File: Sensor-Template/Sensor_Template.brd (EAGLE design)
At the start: 20 x 24.1 mm, 2 parts, among them J1 TWIG-2.0-DIP

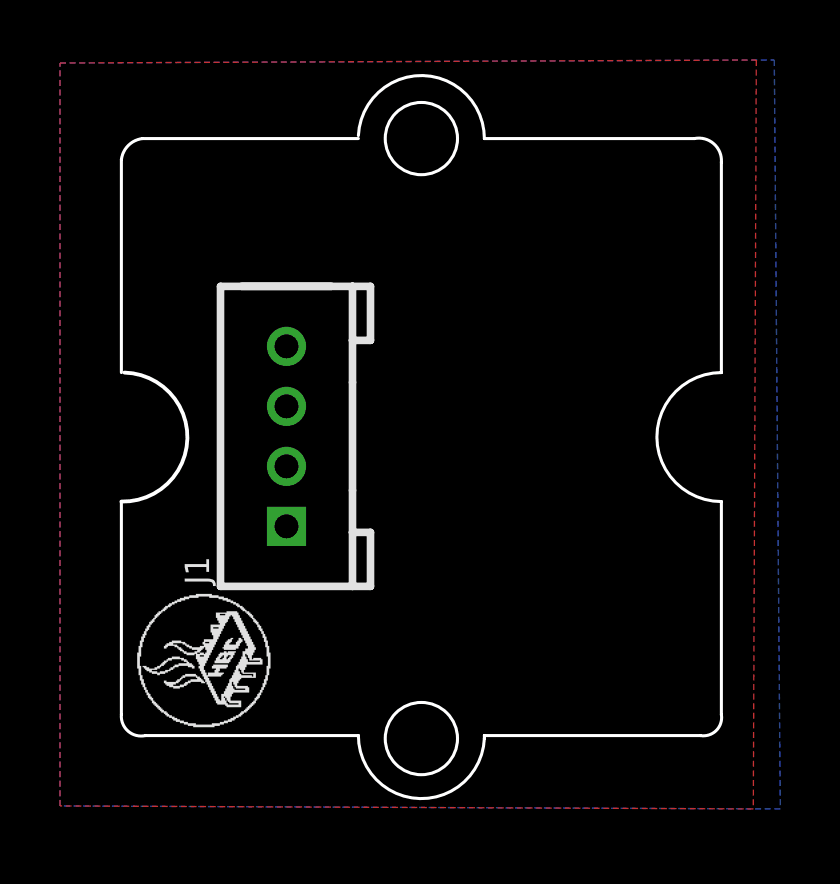
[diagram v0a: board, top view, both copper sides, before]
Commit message: Revised Sensor Template
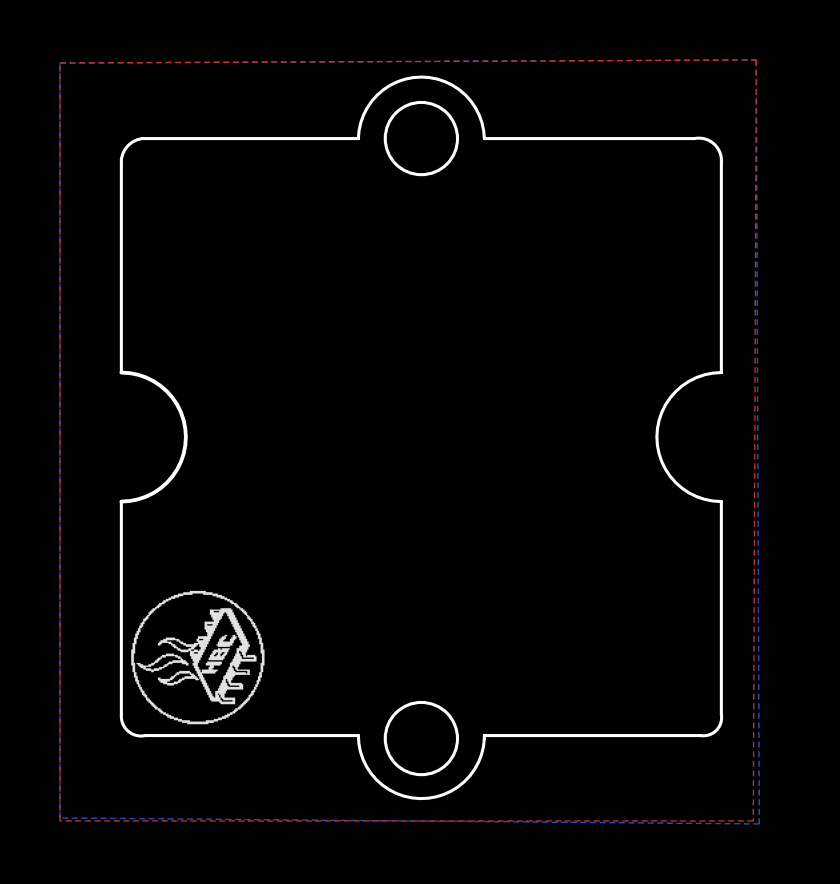
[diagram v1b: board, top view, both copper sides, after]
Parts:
- removed J1: TWIG-2.0-DIP, Connector:2.0_1X4
- moved U$1 0.22 mm to (7.05, 3.00)
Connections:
- removed net DATA: J1.1
- removed net GND: J1.4
- removed net VCC: J1.3
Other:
- outline, holes or cut-outs redrawn
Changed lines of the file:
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@@
 <layer number="43" name="vRestrict" color="2" fill="10" visible="yes" active="yes"/>
 <layer number="44" name="Drills" color="7" fill="1" visible="no" active="yes"/>
-<layer number="45" name="Holes" color="7" fill="1" visible="no" active="yes"/>
+<layer number="45" name="Holes" color="7" fill="1" visible="yes" active="yes"/>
 <layer number="46" name="Milling" color="3" fill="1" visible="no" active="yes"/>
 <layer number="47" name="Measures" color="7" fill="1" visible="no" active="yes"/>
@@
 <layer number="54" name="bGND_GNDA" color="1" fill="9" visible="no" active="no"/>
 <layer number="56" name="wert" color="7" fill="1" visible="no" active="yes"/>
+<layer number="57" name="tCAD" color="7" fill="1" visible="yes" active="yes"/>
+<layer number="59" name="tCarbon" color="7" fill="1" visible="yes" active="yes"/>
+<layer number="60" name="bCarbon" color="7" fill="1" visible="yes" active="yes"/>
 <layer number="90" name="Modules" color="5" fill="1" visible="no" active="no"/>
 <layer number="91" name="Nets" color="2" fill="1" visible="no" active="no"/>
@@
 <layer number="97" name="Info" color="7" fill="1" visible="no" active="no"/>
 <layer number="98" name="Guide" color="6" fill="1" visible="no" active="no"/>
+<layer number="99" name="SpiceOrder" color="7" fill="1" visible="no" active="no"/>
 <layer number="100" name="Muster" color="7" fill="1" visible="no" active="no"/>
 <layer number="101" name="DISIGN_HISTORY" color="3" fill="1" visible="no" active="yes"/>
@@
 <layer number="106" name="bPlate" color="7" fill="1" visible="yes" active="yes"/>
 <layer number="107" name="Crop" color="7" fill="1" visible="yes" active="yes"/>
+<layer number="108" name="centerline" color="7" fill="1" visible="yes" active="yes"/>
+<layer number="109" name="ref-old" color="7" fill="1" visible="yes" active="yes"/>
+<layer number="110" name="fp0" color="7" fill="1" visible="yes" active="yes"/>
+<layer number="111" name="LPC17xx" color="7" fill="1" visible="yes" active="yes"/>
+<layer number="112" name="tSilk" color="7" fill="1" visible="yes" active="yes"/>
+<layer number="113" name="IDFDebug" color="7" fill="1" visible="yes" active="yes"/>
+<layer number="114" name="Badge_Outline" color="7" fill="1" visible="yes" active="yes"/>
+<layer number="115" name="ReferenceISLANDS" color="7" fill="1" visible="yes" active="yes"/>
 <layer number="116" name="Patch_BOT" color="9" fill="4" visible="no" active="yes"/>
+<layer number="118" name="Rect_Pads" color="7" fill="1" visible="yes" active="yes"/>
 <layer number="121" name="_tsilk" color="7" fill="1" visible="no" active="yes"/>
 <layer number="122" name="_bsilk" color="7" fill="1" visible="no" active="yes"/>
+<layer number="123" name="tTestmark" color="7" fill="1" visible="yes" active="yes"/>
+<layer number="124" name="bTestmark" color="7" fill="1" visible="yes" active="yes"/>
+<layer number="125" name="_tNames" color="7" fill="1" visible="yes" active="yes"/>
+<layer number="126" name="_bNames" color="7" fill="1" visible="yes" active="yes"/>
+<layer number="127" name="_tValues" color="7" fill="1" visible="yes" active="yes"/>
+<layer number="128" name="_bValues" color="7" fill="1" visible="yes" active="yes"/>
+<layer number="129" name="Mask" color="7" fill="1" visible="yes" active="yes"/>
+<layer number="131" name="prix" color="7" fill="1" visible="yes" active="yes"/>
+<layer number="132" name="test" color="7" fill="1" visible="yes" active="yes"/>
 <layer number="144" name="DrillLegend" color="7" fill="1" visible="no" active="yes"/>
+<layer number="150" name="Notes" color="7" fill="1" visible="yes" active="yes"/>
 <layer number="151" name="HeatSink" color="14" fill="1" visible="no" active="no"/>
+<layer number="152" name="_bDocu" color="7" fill="1" visible="yes" active="yes"/>
+<layer number="153" name="FabDoc1" color="7" fill="1" visible="yes" active="yes"/>
+<layer number="154" name="FabDoc2" color="7" fill="1" visible="yes" active="yes"/>
+<layer number="155" name="FabDoc3" color="7" fill="1" visible="yes" active="yes"/>
+<layer number="156" name="tAssmbl" color="7" fill="1" visible="yes" active="yes"/>
+<layer number="157" name="bAssmbl" color="7" fill="1" visible="yes" active="yes"/>
+<layer number="199" name="Contour" color="7" fill="1" visible="yes" active="yes"/>
 <layer number="200" name="200bmp" color="1" fill="10" visible="no" active="no"/>
 <layer number="201" name="201bmp" color="2" fill="1" visible="no" active="no"/>
@@
 <layer number="215" name="215bmp" color="7" fill="1" visible="yes" active="yes"/>
 <layer number="216" name="216bmp" color="7" fill="1" visible="yes" active="yes"/>
+<layer number="217" name="217bmp" color="7" fill="1" visible="yes" active="yes"/>
+<layer number="218" name="218bmp" color="7" fill="1" visible="yes" active="yes"/>
+<layer number="219" name="219bmp" color="7" fill="1" visible="yes" active="yes"/>
+<layer number="220" name="220bmp" color="11" fill="1" visible="yes" active="yes"/>
+<layer number="221" name="221bmp" color="7" fill="1" visible="yes" active="yes"/>
+<layer number="223" name="223bmp" color="7" fill="1" visible="yes" active="yes"/>
+<layer number="224" name="224bmp" color="7" fill="1" visible="yes" active="yes"/>
+<layer number="225" name="225bmp" color="7" fill="1" visible="yes" active="yes"/>
+<layer number="226" name="226bmp" color="7" fill="1" visible="yes" active="yes"/>
+<layer number="227" name="227bmp" color="7" fill="1" visible="yes" active="yes"/>
+<layer number="228" name="228bmp" color="7" fill="1" visible="yes" active="yes"/>
+<layer number="229" name="229bmp" color="7" fill="1" visible="yes" active="yes"/>
+<layer number="230" name="230bmp" color="7" fill="1" visible="yes" active="yes"/>
+<layer number="231" name="Eagle3D_PG1" color="7" fill="1" visible="yes" active="yes"/>
+<layer number="232" name="Eagle3D_PG2" color="7" fill="1" visible="yes" active="yes"/>
+<layer number="233" name="Eagle3D_PG3" color="7" fill="1" visible="yes" active="yes"/>
+<layer number="248" name="Housing" color="7" fill="1" visible="yes" active="yes"/>
+<layer number="249" name="Edge" color="7" fill="1" visible="yes" active="yes"/>
 <layer number="250" name="Descript" color="3" fill="1" visible="no" active="no"/>
 <layer number="251" name="SMDround" color="12" fill="11" visible="no" active="no"/>
 <layer number="254" name="OrgLBR" color="13" fill="1" visible="no" active="no"/>
+<layer number="255" name="logo" color="7" fill="1" visible="yes" active="yes"/>
 </layers>
 <board>
@@
 <wire x1="14.4" y1="22.5" x2="21.4" y2="22.5" width="0.1016" layer="20"/>
 <wire x1="22.3" y1="21.7" x2="22.3" y2="14.7" width="0.1016" layer="20"/>
-<wire x1="14.4" y1="22.5" x2="10.2" y2="22.6" width="0.1016" layer="20" curve="177.278311"/>
+<wire x1="14.4" y1="22.5" x2="10.2" y2="22.5" width="0.1016" layer="20" curve="177.278311"/>
 <wire x1="22.3" y1="21.7" x2="21.4" y2="22.5" width="0.1016" layer="20" curve="106.260205"/>
 <wire x1="22.3" y1="10.4" x2="22.3" y2="3.3" width="0.1016" layer="20"/>
@@
 <circle x="12.3" y="2.5" radius="1.204159375" width="0.1016" layer="20"/>
 <circle x="12.3" y="22.5" radius="1.204159375" width="0.1016" layer="20"/>
-<wire x1="2.4" y1="14.7" x2="2.3" y2="10.4" width="0.127" layer="20" curve="-180"/>
+<wire x1="2.3" y1="14.7" x2="2.3" y2="10.4" width="0.127" layer="20" curve="-180"/>
+<hole x="12.3" y="22.5" drill="2.4"/>
+<hole x="12.3" y="2.5" drill="2.4"/>
 </plain>
 <attributes>
@@
 </autorouter>
 <elements>
-<element name="J1" library="Connector" package="2.0_1X4" value="TWIG-2.0-DIP" x="7.804" y="12.573" rot="R90"/>
-<element name="U$1" library="HalfBakedCircuits" package="HBC-LOGO-SMALL" value="HBC-LOGO-SMALL" x="7.25" y="2.9" rot="R90"/>
+<element name="U$1" library="HalfBakedCircuits" package="HBC-LOGO-SMALL" value="HBC-LOGO-SMALL" x="7.05" y="3" rot="R90"/>
 </elements>
 <signals>
-<signal name="DATA">
-<contactref element="J1" pad="1"/>
-</signal>
-<signal name="VCC">
-<contactref element="J1" pad="3"/>
-</signal>
 <signal name="GND">
-<contactref element="J1" pad="4"/>
 <polygon width="0.254" layer="16" isolate="0.3048">
-<vertex x="24.264" y="0.154"/>
-<vertex x="0.254" y="0.254"/>
+<vertex x="23.564" y="-0.346"/>
+<vertex x="0.254" y="-0.146"/>
 <vertex x="0.254" y="25.019"/>
-<vertex x="24.064" y="25.119"/>
+<vertex x="23.464" y="25.119"/>
 </polygon>
 <polygon width="0.254" layer="1" isolate="0.3048">
-<vertex x="23.364" y="0.154"/>
-<vertex x="0.254" y="0.254"/>
+<vertex x="23.364" y="-0.246"/>
+<vertex x="0.254" y="-0.246"/>
 <vertex x="0.254" y="25.019"/>
 <vertex x="23.464" y="25.119"/>
